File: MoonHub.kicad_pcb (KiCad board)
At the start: 4 copper layers, 102 x 16.5 mm, 44 parts, among them J1 X1224WRS-04-LPV01, U1 AP22818AKBWT-7, U2 SRV05-4, U3 SRV05-4, U4 CH334U, U5 SRV05-4, U6 SRV05-4, U7 SRV05-4, Y1 12MHz

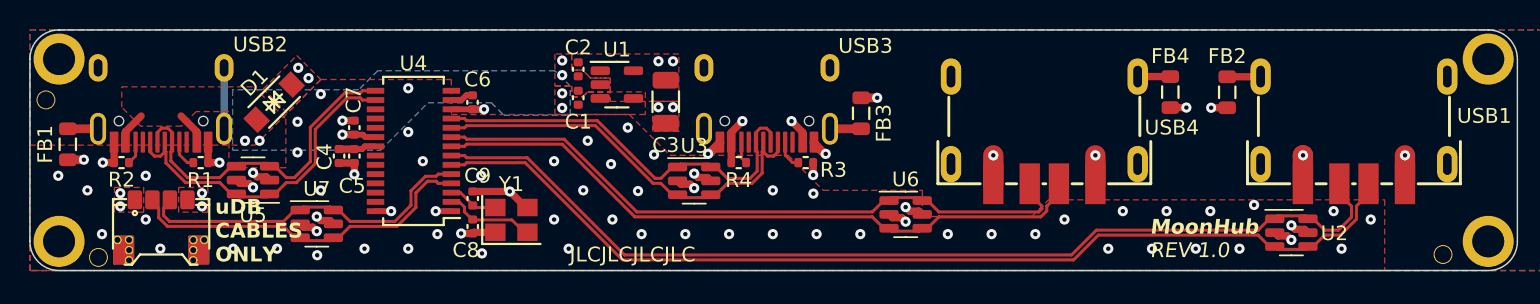
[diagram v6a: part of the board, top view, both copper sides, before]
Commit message: change usb esd array
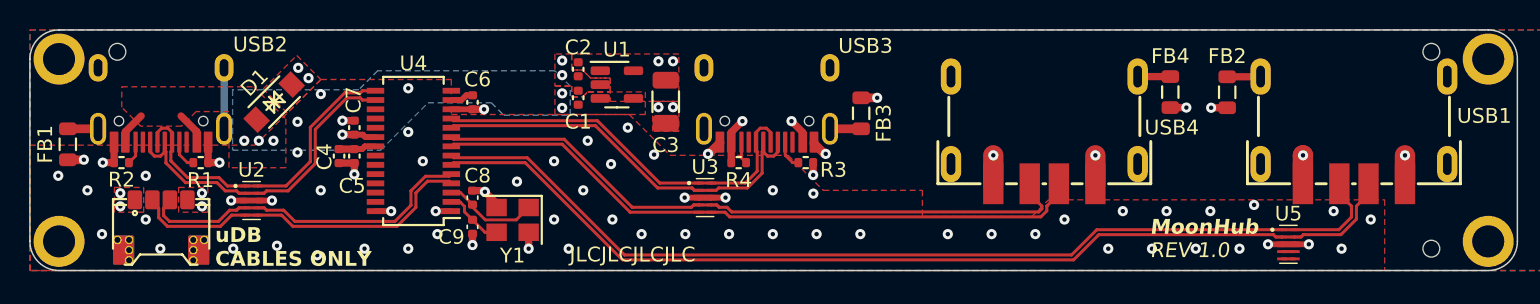
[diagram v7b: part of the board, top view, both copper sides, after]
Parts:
- removed the REF** at (91.5, 12.2)
- removed U6, U7: SRV05-4, Package_TO_SOT_SMD:SOT-23-6
- added REF**: OSHW-Logo_11.4x12mm_SilkScreen, Symbol:OSHW-Logo_11.4x12mm_SilkScreen, B.Cu at (19.3, 10.0)
- C8, C9: value 12p -> 20p
- U2, U3, U5: value SRV05-4 -> H5VU25U; footprint Package_TO_SOT_SMD:SOT-23-6 -> MoonHub:DFN2510
- moved H6 92.5 mm to (96.1, 1.50)
- moved U2 71.3 mm to (15.2, 11.7), turned to -90 degrees
- moved U5 71.1 mm to (86.3, 14.7), turned to -90 degrees
- moved G*** 20.9 mm to (29.7, 1.90)
- moved H5 5.91 mm to (6.00, 1.50)
- moved C8 1.98 mm to (30.4, 11.5), turned to 90 degrees
- moved C9 1.94 mm to (30.4, 13.5), turned to -90 degrees
- moved U3 1.37 mm to (46.3, 11.5), turned to -90 degrees
- moved H7 0.89 mm to (96.1, 15.0)
- moved Y1 0.09 mm to (33.1, 13.0), turned to 180 degrees
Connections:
- C8 pad 1: Net-(U4-XO) -> Net-(U4-XI)
- C9 pad 1: Net-(U4-XI) -> Net-(U4-XO)
- U2 pad 1: /USB3_D+ -> /USBU_D-
- U2 pad 2: GND -> /USBU_D+
- U2 pad 3: /USB3_D- -> GND
- U2 pad 4: /USB3_D- -> /USB4_D+
- U2 pad 5: VBUS -> /USB4_D-
- U2 pad 6: /USB3_D+ -> /USB4_D-
- U3 pad 2: GND -> /USB1_D-
- U3 pad 3: /USB1_D- -> GND
- U3 pad 4: /USB1_D- -> /USB2_D+
- U3 pad 5: VBUS -> /USB2_D-
- U3 pad 6: /USB1_D+ -> /USB2_D-
- U5 pad 1: /USBU_D+ -> /USB3_D+
- U5 pad 2: GND -> /USB3_D-
- U5 pad 3: /USBU_D- -> GND
- U5 pad 4: /USBU_D- -> unconnected-(U5-D2+-Pad4)
- U5 pad 5: VBUS -> unconnected-(U5-D2--Pad5)
- U5 pad 6: /USBU_D+ -> unconnected-(U5-D2--Pad5)
- Y1 pad 1: GND -> Net-(U4-XI)
- Y1 pad 2: Net-(U4-XO) -> GND
- Y1 pad 3: GND -> Net-(U4-XO)
- Y1 pad 4: Net-(U4-XI) -> GND
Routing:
- net VBUS: track 16.4 -> 9.67 mm, vias 14 -> 9
- net Net-(U4-XI): track 3.46 -> 6.53 mm
- net Net-(U4-XO): track 6.27 -> 4.18 mm
- net GND: track 35.4 -> 33.9 mm
- net unconnected-(U5-D2--Pad5): track 0.00 -> 0.88 mm
- net unconnected-(U5-D2+-Pad4): track 0.00 -> 0.88 mm
- net /USB2_D-: track 46.1 -> 45.3 mm
- net /USB3_D+: track 69.1 -> 68.3 mm
- net /USB3_D-: track 69.6 -> 68.9 mm
- net /USB2_D+: track 45.6 -> 44.9 mm
- net /USB1_D+: track 28.3 -> 27.7 mm
- net +5V: vias 5 -> 6
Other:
- board text added: "S/N"
- board text added: "a design by"

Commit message: remove ferrites
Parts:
- removed FB1, FB2, FB3, FB4: 100R@100MHz, Inductor_SMD:L_0805_2012Metric
- C1: value 1u -> 10u; footprint Capacitor_SMD:C_0402_1005Metric -> Capacitor_SMD:C_0805_2012Metric
- D1: value SMF6.0CA -> SMAJ5.0A; footprint MoonHub:SOD-123FL_L2.8-W1.8-LS3.7-BI -> Diode_SMD:D_SMA
- H1, H3, H4: value MountingHole_Pad -> MountingHole; footprint MoonHub:Generic-Mounthole -> MountingHole:MountingHole_2.2mm_M2_ISO7380
- moved H3 98.0 mm to (100.0, 14.5)
- moved H4 98.0 mm to (2.00, 14.5)
- moved H5 5.71 mm to (1.20, 4.60)
- moved H6 5.63 mm to (100.8, 4.60)
- moved D1 1.66 mm to (18.4, 4.80), turned to 45 degrees
- moved H7 1.22 mm to (97.3, 15.2)
- moved C2 0.94 mm to (37.1, 1.90), turned to 180 degrees
- moved R3 0.77 mm to (52.5, 9.38)
- moved C1 0.69 mm to (37.0, 4.30)
- moved R1 0.28 mm to (11.7, 9.38)
- moved R2 0.28 mm to (6.28, 9.38)
- moved R4 0.28 mm to (48.6, 9.38)
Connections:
- D1 pad 1: GND -> +5V
- D1 pad 2: +5V -> GND
- J1 pad MP: GND -> GNDPWR
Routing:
- net GNDPWR: track 12.9 -> 4.18 mm
- net GND: track 33.9 -> 30.0 mm, vias 84 -> 78
- net VBUS: track 9.67 -> 10.8 mm, vias 9 -> 8
- net +5V: vias 6 -> 5
